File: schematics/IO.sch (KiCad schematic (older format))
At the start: 80 parts, among them J2 Outputs, J8 Power Pins, Q1 MMBT3906, U10 TL082, U11 TL082, U12 6S21, U12 MCP4728, U13 TL082, U16 TL082, U6 DS1307Z+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

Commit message: refactor: redraw mcu
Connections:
- net SQ3 renamed SQR3_
- net SQ4 renamed SQR4_
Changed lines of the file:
@@
 $EndComp
 Text GLabel 1225 5250 0    40   Input ~ 0
-SQ4
+SQR4_
 $Comp
 L PSLab-rescue:GND-RESCUE-proto1 #PWR071
@@
 SINE2
 Text GLabel 1200 6800 0    40   Input ~ 0
-SQ3
+SQR3_
 $Comp
 L PSLab-rescue:GND-RESCUE-proto1 #PWR078

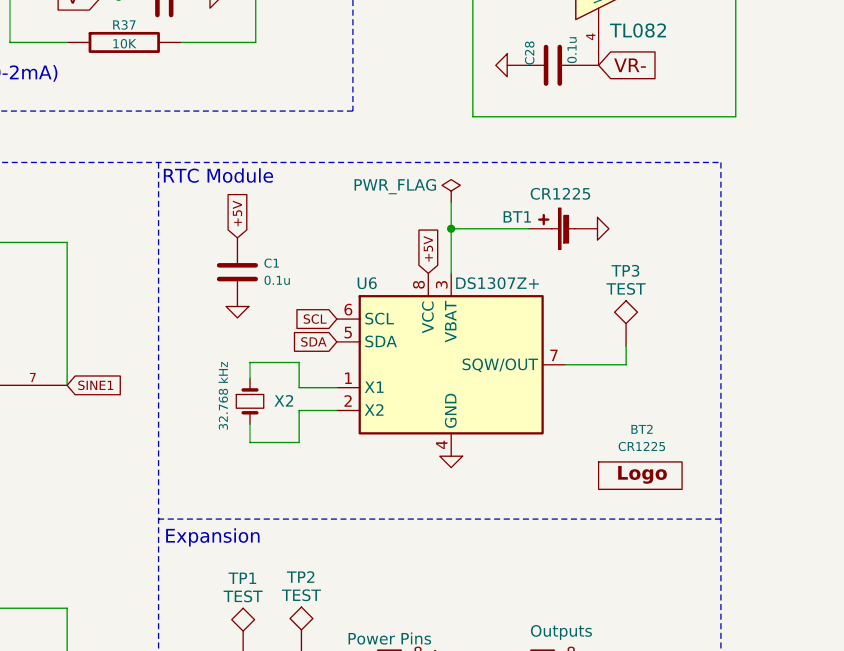
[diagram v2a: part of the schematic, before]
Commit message: refactor: redraw rtc module
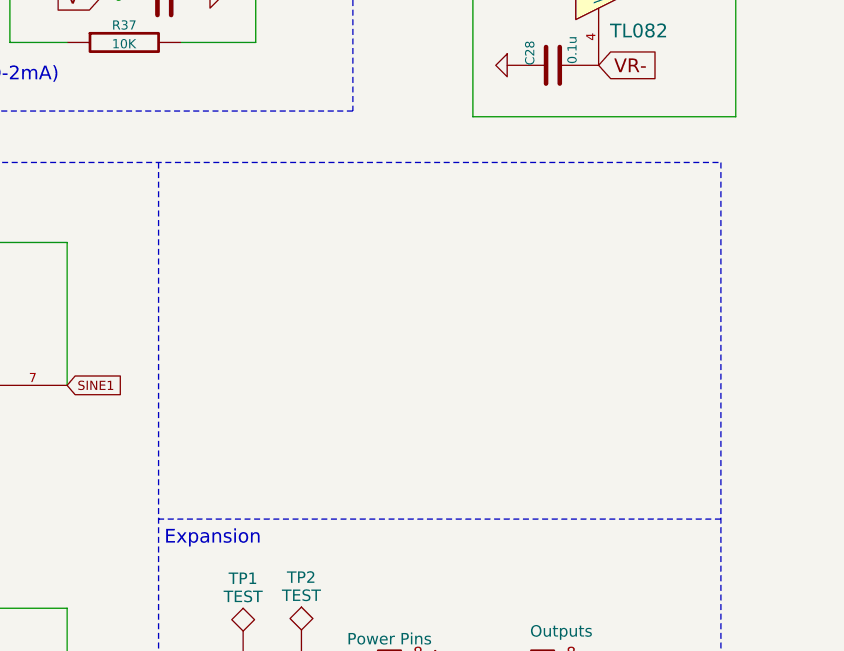
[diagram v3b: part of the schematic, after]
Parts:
- removed BT1: CR1225, Battery:BatteryHolder_LINX_BAT-HLD-012-SMT, symbol Device:Battery_Cell
- removed BT2: CR1225, Battery:Battery_CR1225, symbol PSLab:Logos
- removed C1: 0.1u, Capacitor_SMD:C_0603_1608Metric, symbol Device:C
- removed TP3: TEST, TestPoint:TestPoint_Pad_1.0x1.0mm, symbol PSLab-rescue:TEST
- removed U6: DS1307Z+, Package_SO:SOIC-8_3.9x4.9mm_P1.27mm, symbol Timer_RTC:DS1307Z+
- removed X2: 32.768 kHz, Crystal:Crystal_SMD_3215-2Pin_3.2x1.5mm, symbol Device:Crystal_Small
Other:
- note removed: "RTC Module"
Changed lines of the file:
@@
 Wire Notes Line
 	6760 4175 6760 7450
-Text Notes 4315 4280 0    60   ~ 0
-RTC Module
-$Comp
-L Timer_RTC:DS1307Z+ U6
-U 1 1 5CA94FBE
-P 5580 5060
-F 0 "U6" H 5165 5415 50  0000 L CNN
-F 1 "DS1307Z+" H 5595 5415 50  0000 L CNN
-F 2 "Package_SO:SOIC-8_3.9x4.9mm_P1.27mm" H 5580 4560 50  0001 C CNN
-F 3 "https://eu.mouser.com/datasheet/2/256/DS1307-1513036.pdf" H 5580 5060 50  0001 C CNN
-F 4 "Real Time Clock IC" H 5580 5060 50  0001 C CNN "Description"
-F 5 "DS1307Z+" H 5580 5060 50  0001 C CNN "PartNumber"
-F 6 "3.69" H 5580 5060 50  0001 C CNN "Price"
-F 7 "DS1307Z+" H 5580 5060 50  0001 C CNN "Mfr No."
-	1    5580 5060
-	1    0    0    -1
-$EndComp
-$Comp
-L Device:Crystal_Small X2
-U 1 1 5CA951B5
-P 4700 5220
-F 0 "X2" V 4700 5325 50  0000 L CNN
-F 1 "32.768 kHz" H 4525 5105 39  0000 L CNN
-F 2 "Crystal:Crystal_SMD_3215-2Pin_3.2x1.5mm" H 4700 5220 50  0001 C CNN
-F 3 "https://eu.mouser.com/datasheet/2/3/ABS07-166-32.768kHz-T-1359238.pdf" H 4700 5220 50  0001 C CNN
-F 4 "ABS07-166-32.768KHZ-T" V 4700 5220 50  0001 C CNN "PartNumber"
-F 5 "0.66" V 4700 5220 50  0001 C CNN "Price"
-F 6 "RTC Crystal 32.768 kHz" V 4700 5220 50  0001 C CNN "Description"
-F 7 "ABS07-166-32.768KHZ-T" H 4700 5220 50  0001 C CNN "Mfr No."
-	1    4700 5220
-	0    1    1    0
-$EndComp
-Wire Wire Line
-	4700 5120 4700 5050
-Wire Wire Line
-	4700 5050 4915 5050
-Wire Wire Line
-	4915 5050 4915 5160
-Wire Wire Line
-	4915 5160 5080 5160
-Wire Wire Line
-	4700 5320 4700 5400
-Wire Wire Line
-	4700 5400 4915 5400
-Wire Wire Line
-	4915 5400 4915 5260
-Wire Wire Line
-	4915 5260 5080 5260
-$Comp
-L PSLab-rescue:GND-RESCUE-proto1 #PWR?
-U 1 1 5CAA467A
-P 5580 5460
-AR Path="/5CAA467A" Ref="#PWR?"  Part="1"
-AR Path="/54260FB5/5CAA467A" Ref="#PWR010"  Part="1"
-F 0 "#PWR010" H 5580 5460 30  0001 C CNN
-F 1 "GND" H 5580 5390 30  0001 C CNN
-F 2 "" H 5580 5460 60  0000 C CNN
-F 3 "" H 5580 5460 60  0000 C CNN
-	1    5580 5460
-	-1   0    0    -1
-$EndComp
-$Comp
-L Device:Battery_Cell BT1
-U 1 1 5CAA5A87
-P 6120 4465
-F 0 "BT1" V 6170 4716 50  0000 C CNN
-F 1 "CR1225" V 6271 4526 50  0000 C CNN
-F 2 "Battery:BatteryHolder_LINX_BAT-HLD-012-SMT" V 6120 4525 50  0001 C CNN
-F 3 "https://eu.mouser.com/datasheet/2/238/bat-hld-012-smt-1659340.pdf" V 6120 4525 50  0001 C CNN
-F 4 "Coin cell battery holder (CR1225/1216)" V 6120 4465 50  0001 C CNN "Description"
-F 5 "BAT-HLD-012-SMT" V 6120 4465 50  0001 C CNN "PartNumber"
-F 6 "0.29" V 6120 4465 50  0001 C CNN "Price"
-F 7 "BAT-HLD-012-SMT" H 6120 4465 50  0001 C CNN "Mfr No."
-	1    6120 4465
-	0    -1   -1   0
-$EndComp
-Wire Wire Line
-	5920 4465 5580 4465
-Wire Wire Line
-	5580 4465 5580 4660
-$Comp
-L PSLab-rescue:GND-RESCUE-proto1 #PWR?
-U 1 1 5CAAD598
-P 6220 4465
-AR Path="/5CAAD598" Ref="#PWR?"  Part="1"
-AR Path="/54260FB5/5CAAD598" Ref="#PWR021"  Part="1"
-F 0 "#PWR021" H 6220 4465 30  0001 C CNN
-F 1 "GND" H 6220 4395 30  0001 C CNN
-F 2 "" H 6220 4465 60  0000 C CNN
-F 3 "" H 6220 4465 60  0000 C CNN
-	1    6220 4465
-	0    -1   1    0
-$EndComp
-Text GLabel 5080 4860 0    40   Input ~ 0
-SCL
-Text GLabel 5080 4960 0    40   Input ~ 0
-SDA
-Text GLabel 5480 4660 1    40   Input ~ 0
-+5V
-Wire Wire Line
-	5580 4350 5580 4465
-Connection ~ 5580 4465
-$Comp
-L power:PWR_FLAG #FLG0101
-U 1 1 5CAE0079
-P 5580 4350
-F 0 "#FLG0101" H 5580 4425 50  0001 C CNN
-F 1 "PWR_FLAG" H 5335 4425 50  0000 C CNN
-F 2 "" H 5580 4350 50  0001 C CNN
-F 3 "~" H 5580 4350 50  0001 C CNN
-	1    5580 4350
-	1    0    0    -1
-$EndComp
 $Comp
 L Connector_Generic:Conn_01x08 J2
@@
 	6515 6360 6515 6860
 Connection ~ 6515 6860
-$Comp
-L Device:C C1
-U 1 1 5EF248D3
-P 4645 4655
-F 0 "C1" H 4760 4693 39  0000 L CNN
-F 1 "0.1u" H 4760 4618 39  0000 L CNN
-F 2 "Capacitor_SMD:C_0603_1608Metric" H 4683 4505 50  0001 C CNN
-F 3 "https://eu.mouser.com/datasheet/2/212/KEM_C1002_X7R_SMD-1102033.pdf" H 4645 4655 50  0001 C CNN
-F 4 "16V 10%" H 4645 4655 50  0001 C CNN "Description"
-F 5 "C0603C104J4RACTU" H 4645 4655 50  0001 C CNN "Mfr No."
-F 6 "0.15" H 4645 4655 50  0001 C CNN "Price"
-F 7 "C0603C104J4RACTU" H 4645 4655 50  0001 C CNN "PartNumber"
-	1    4645 4655
-	1    0    0    -1
-$EndComp
-$Comp
-L PSLab-rescue:GND-RESCUE-proto1 #PWR?
-U 1 1 5EF25336
-P 4645 4805
-AR Path="/5EF25336" Ref="#PWR?"  Part="1"
-AR Path="/54260FB5/5EF25336" Ref="#PWR032"  Part="1"
-F 0 "#PWR032" H 4645 4805 30  0001 C CNN
-F 1 "GND" H 4645 4735 30  0001 C CNN
-F 2 "" H 4645 4805 60  0000 C CNN
-F 3 "" H 4645 4805 60  0000 C CNN
-	1    4645 4805
-	-1   0    0    -1
-$EndComp
-Text GLabel 4645 4505 1    40   Input ~ 0
-+5V
-$Comp
-L PSLab-rescue:TEST TP?
-U 1 1 5EF27AA3
-P 6345 4980
-AR Path="/5EF27AA3" Ref="TP?"  Part="1"
-AR Path="/54260FB5/5EF27AA3" Ref="TP3"  Part="1"
-F 0 "TP3" H 6345 5280 50  0000 C BNN
-F 1 "TEST" H 6345 5230 50  0000 C CNN
-F 2 "TestPoint:TestPoint_Pad_1.0x1.0mm" H 6345 4980 50  0001 C CNN
-F 3 "" H 6345 4980 50  0001 C CNN
-	1    6345 4980
-	1    0    0    -1
-$EndComp
-Wire Wire Line
-	6080 5060 6345 5060
-Wire Wire Line
-	6345 5060 6345 4980
-$Comp
-L PSLab:Logos BT2
-U 1 1 5EF40E40
-P 6415 5535
-F 0 "BT2" H 6415 5726 39  0000 C CNN
-F 1 "CR1225" H 6415 5651 39  0000 C CNN
-F 2 "Battery:Battery_CR1225" H 6415 5535 60  0001 C CNN
-F 3 "https://data.energizer.com/PDFs/cr1225.pdf" H 6415 5535 60  0001 C CNN
-F 4 "3V 12.5mm x 2.5 mm 48 mAh" H 6415 5535 50  0001 C CNN "Description"
-F 5 "CR1225" H 6415 5535 50  0001 C CNN "PartNumber"
-F 6 "1" H 6415 5535 50  0001 C CNN "Price"
-	1    6415 5535
-	1    0    0    -1
-$EndComp
 $EndSCHEMATC

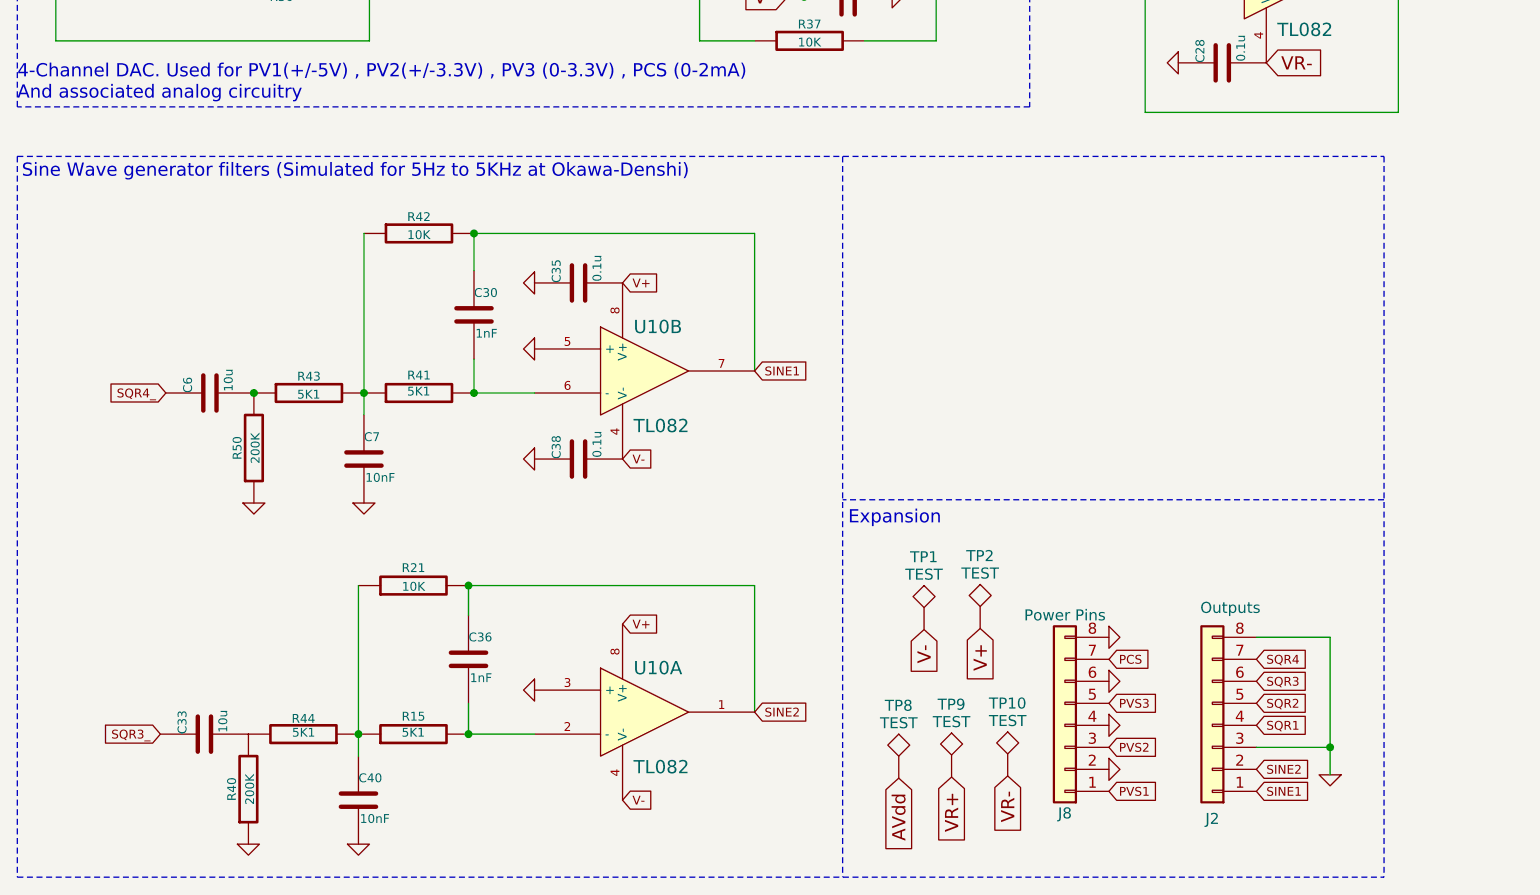
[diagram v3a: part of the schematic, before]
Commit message: refactor: sine wave generator
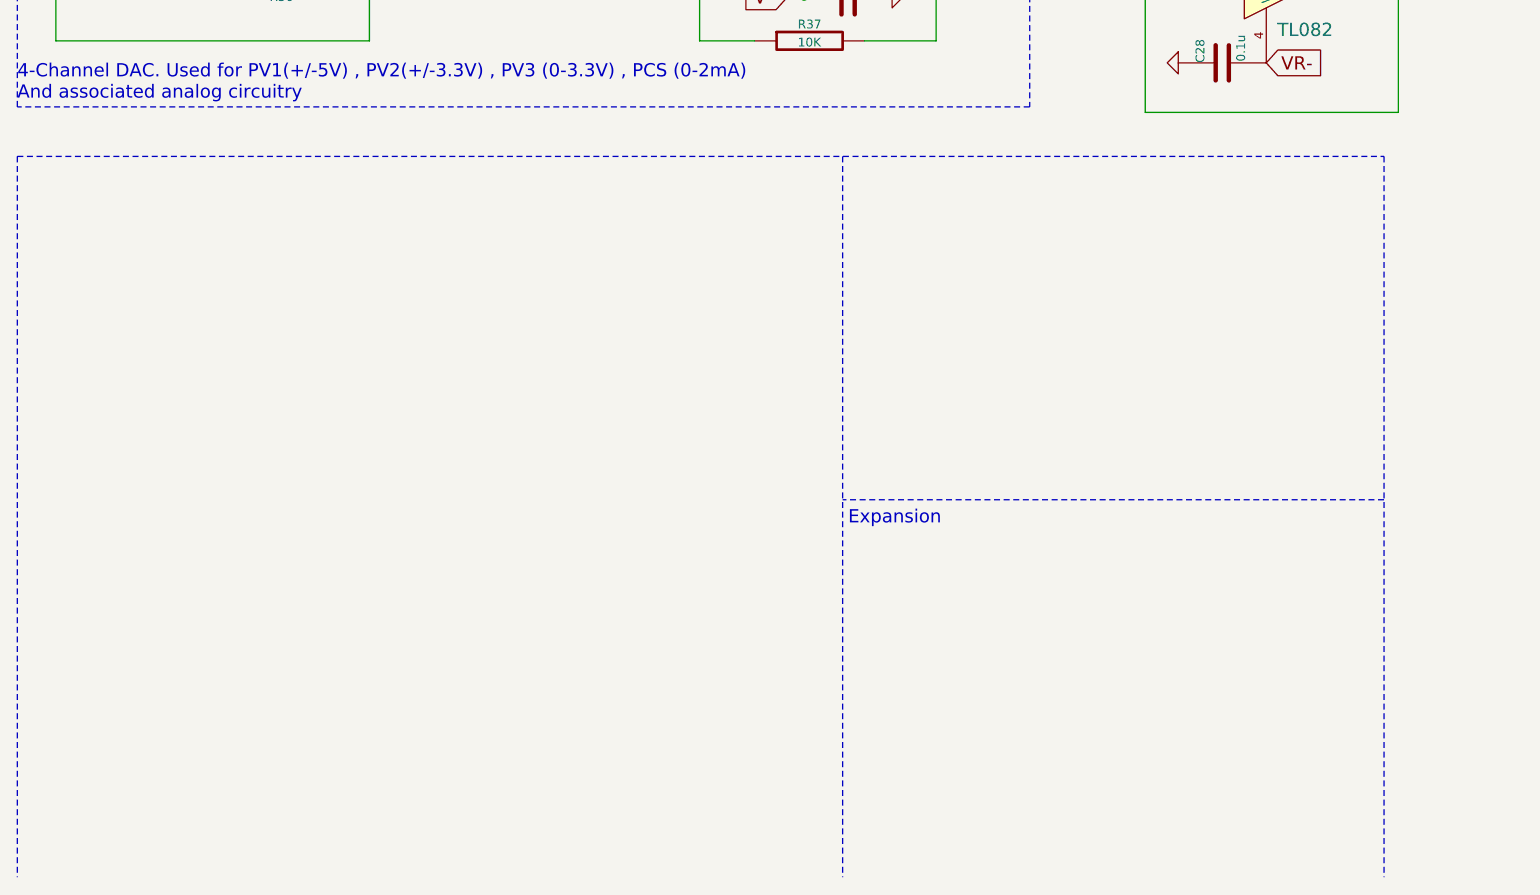
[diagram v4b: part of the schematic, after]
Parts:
- removed C30, C36: 1nF, Capacitor_SMD:C_0603_1608Metric, symbol PSLab-rescue:C-RESCUE-proto1
- removed C33, C6: 10u, Capacitor_SMD:C_0603_1608Metric, symbol PSLab-rescue:C-RESCUE-proto1
- removed C35, C38: 0.1u, Capacitor_SMD:C_0603_1608Metric, symbol PSLab-rescue:C-RESCUE-proto1
- removed C40, C7: 10nF, Capacitor_SMD:C_0603_1608Metric, symbol PSLab-rescue:C-RESCUE-proto1
- removed J2: Outputs, Connector_PinSocket_2.54mm:PinSocket_1x08_P2.54mm_Vertical, symbol Connector_Generic:Conn_01x08
- removed J8: Power Pins, Pin_Headers:Pin_Header_Straight_1x08_Pitch2.54mm, symbol PSLab-rescue:Conn_01x08
- removed R15, R41, R43, R44: 5K1, Resistor_SMD:R_0603_1608Metric, symbol PSLab-rescue:R-RESCUE-proto1
- removed R21, R42: 10K, Resistor_SMD:R_0603_1608Metric, symbol PSLab-rescue:R-RESCUE-proto1
- removed R40, R50: 200K, Resistor_SMD:R_0603_1608Metric, symbol PSLab-rescue:R-RESCUE-proto1
- removed TP1, TP10, TP2, TP8, TP9: TEST, TestPoint:TestPoint_Pad_1.0x1.0mm, symbol PSLab-rescue:TEST
- removed U13: TL082, Package_SO:SOIC-8_3.9x4.9mm_P1.27mm, symbol PSLab-rescue:TL082-RESCUE-proto1
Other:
- note removed: "Sine Wave generator filters (Simulated for 5Hz to 5KHz at Okawa-Denshi)"

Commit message: refactor: power source
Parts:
- removed C24, C27, C32: 0.1u, Capacitor_SMD:C_0603_1608Metric, symbol PSLab-rescue:C-RESCUE-proto1
- removed Q1: MMBT3906, TO_SOT_Packages_SMD:SOT-23, symbol PSLab-rescue:MMBT3906
- removed R18, R19, R25, R35, R37: 10K, Resistor_SMD:R_0603_1608Metric, symbol PSLab-rescue:R-RESCUE-proto1
- removed R26: 5K1, Resistor_SMD:R_0603_1608Metric, symbol PSLab-rescue:R-RESCUE-proto1
- removed R27, R36: 1K, Resistor_SMD:R_0603_1608Metric, symbol PSLab-rescue:R-RESCUE-proto1
- removed U12: MCP4728, Package_SO:MSOP-10_3x3mm_P0.5mm, symbol PSLab:MCP4728-RESCUE-PSLab
- removed U7: LM324, Package_SO:SOIC-14_3.9x8.7mm_P1.27mm, symbol PSLab-rescue:LM324-RESCUE-proto1
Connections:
- no-connect marks 1 -> 0
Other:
- note removed: "4-Channel DAC. Used for PV1(+/-5V) , PV2(+/-3.3V) , PV3 (0-3.3V) , PCS (0-2mA)\nAnd associated analog circuitry"
- note removed: "Expansion"

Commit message: refactor: oscilloscope
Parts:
- removed C22, C25, C26, C28, C31, C34, C37, C39, C41: 0.1u, Capacitor_SMD:C_0603_1608Metric, symbol PSLab-rescue:C-RESCUE-proto1
- removed C23, C29: 0.5p, Capacitor_SMD:C_0603_1608Metric, symbol PSLab-rescue:C-RESCUE-proto1
- removed C43: 1u, Capacitor_SMD:C_0603_1608Metric, symbol PSLab-rescue:C-RESCUE-proto1
- removed R14, R16, R17, R22, R23, R28, R29, R31, R32, R33, R38, R39: 10K, Resistor_SMD:R_0603_1608Metric, symbol PSLab-rescue:R-RESCUE-proto1
- removed R20, R30, R46: 200K, Resistor_SMD:R_0603_1608Metric, symbol PSLab-rescue:R-RESCUE-proto1
- removed R24, R34, R45: 1M, Resistor_SMD:R_0603_1608Metric, symbol PSLab-rescue:R-RESCUE-proto1
- removed R47: 1K, Resistor_SMD:R_0603_1608Metric, symbol PSLab-rescue:R-RESCUE-proto1
- removed U10, U16, U8: TL082, Package_SO:SOIC-8_3.9x4.9mm_P1.27mm, symbol PSLab-rescue:TL082-RESCUE-proto1
- removed U11: TL082, Package_SO:SOIC-8_3.9x4.9mm_P1.27mm, symbol PSLab-rescue:MCP6S21A
- removed U12: 6S21, Package_SO:SOIC-8_3.9x4.9mm_P1.27mm, symbol PSLab-rescue:MCP6S21A
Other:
- note removed: "Signal Processing"
